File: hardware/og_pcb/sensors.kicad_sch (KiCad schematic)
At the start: 17 parts, among them U13 INA219AxD, U14 TMP1075DSG, U7 LSM303AGRTR

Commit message: updated pcb work in progress (incomplete)
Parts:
- removed C12, C14: 100nF, Capacitor_SMD:C_0402_1005Metric, symbol Device:C
- removed C13: 220nF, Capacitor_SMD:C_0402_1005Metric, symbol Device:C
- removed C41: 0.01uF, Capacitor_SMD:C_0402_1005Metric, symbol Device:C
- removed R10, R11, R18, R7: 10k, Resistor_SMD:R_0402_1005Metric, symbol Device:R
- removed R19, R20, R21: 5k, Resistor_SMD:R_0402_1005Metric, symbol Device:R
- removed U14: TMP1075DSG, Package_SON:WSON-8-1EP_2x2mm_P0.5mm_EP0.9x1.6mm_ThermalVias, symbol Sensor_Temperature:TMP1075DSG
- removed U7: LSM303AGRTR, 1my_footprints:SON_03AGRTR_STM-L, symbol 1my_symbol:LSM303AGR
- added C44: 0.01uF, Capacitor_SMD:C_0402_1005Metric, symbol Device:C
- added R24, R25, R26: 5k, Resistor_SMD:R_0402_1005Metric, symbol Device:R
- added U15: TMP1075DSG, Package_SON:WSON-8-1EP_2x2mm_P0.5mm_EP0.9x1.6mm_ThermalVias, symbol Sensor_Temperature:TMP1075DSG
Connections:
- net +3.3V: now also C44.1, R24.1, R25.1, R26.1, U15.8 (V+)
- net GND: now also C44.2, U15.4 (GND), U15.9 (EP)
- net Temp Alert: now also R26.2, U15.3 (ALERT)
- net at R22.1: now also U15.7 (A0)
- net Power Monitor SCL renamed SCL1
- net Power Monitor SDA renamed SDA1
- new net SCL0: R25.2, U15.2 (SCL), U15.5 (A2)
- new net SDA0: R24.2, U15.1 (SDA), U15.6 (A1)
- no-connect marks 3 -> 0
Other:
- note added: "add shunt resistor"
- note removed: "(pullup resistors)"
- note removed: "Inertial Measurement Unit"
- moved on the sheet: R22

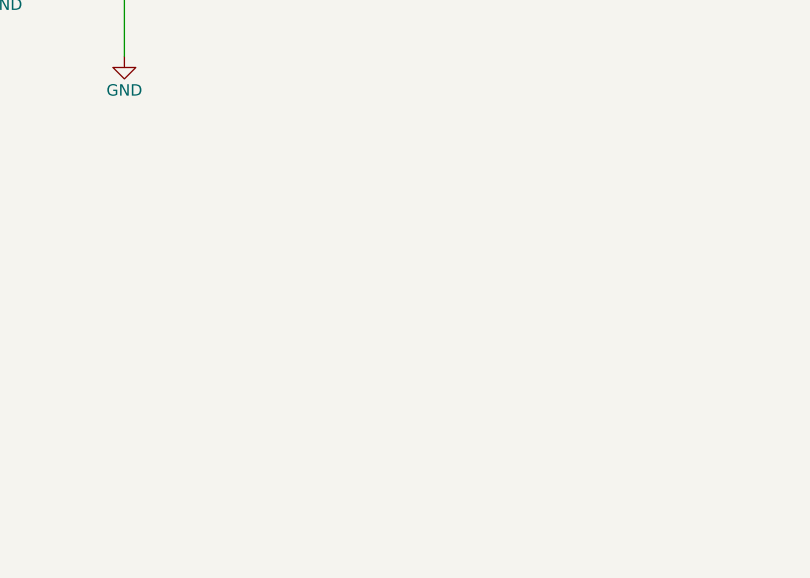
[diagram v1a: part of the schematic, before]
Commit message: updated pcb v2 progress
reimplemented spi microSD, changed power monitor to model with internal shunt resistor, changed power supply from usbc to barrel jack, reconnected vbus to microusb, modified spi and i2c connections (2 i2c connections, 2 spi connections), removed RF module & IMU.

to do:
- find/create footprints for new parts
- verify implementation by reviewing datasheets again
- implement coax connector for analog connection to cosmic watch
- implement gps receiver (must do more research; implement one well-known/documented/used b4)
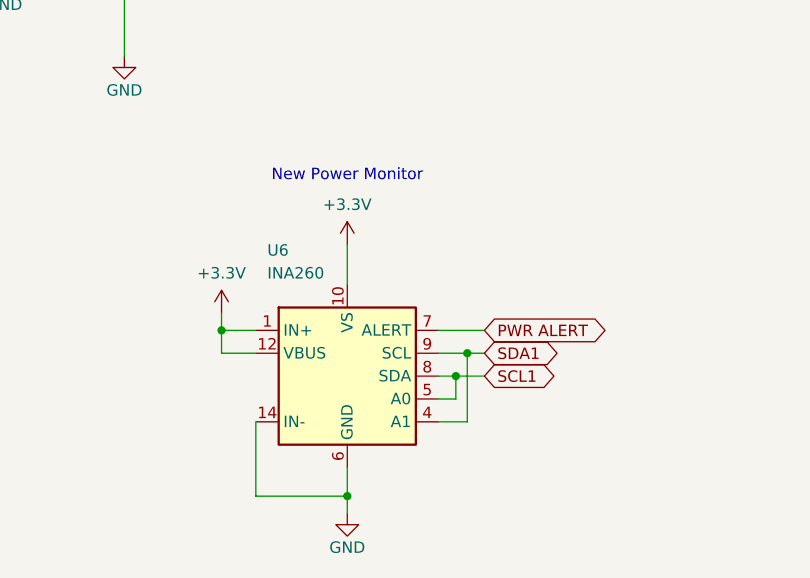
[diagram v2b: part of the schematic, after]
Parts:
- added U6: INA260, Package_SO:TSSOP-16_4.4x5mm_P0.65mm, symbol Sensor:INA260
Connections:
- net +3.3V: now also U6.1 (IN+), U6.10 (VS), U6.12 (VBUS), U6.2 (IN+), U6.3 (IN+)
- net GND: now also U6.11 (GND), U6.14 (IN-), U6.15 (IN-), U6.16 (IN-), U6.6 (GND)
- net SCL1: now also U6.5 (A0), U6.8 (SDA)
- net SDA1: now also U6.4 (A1), U6.9 (SCL)
- new net PWR ALERT: U6.7 (ALERT)
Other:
- note added: "New Power Monitor"

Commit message: new preliminary demo pcb
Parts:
- added C20: 10uF, Capacitor_SMD:C_0402_1005Metric, symbol Device:C
- added C21: 0.1uf, Capacitor_SMD:C_0402_1005Metric, symbol Device:C
- added FB1: FerriteBead, symbol Device:FerriteBead
- added J2: Conn_Coaxial, Connector_Coaxial:MMCX_Molex_73415-1471_Vertical, symbol Connector:Conn_Coaxial
- added R27: 0.002, Resistor_SMD:R_0402_1005Metric, symbol Device:R
- added U1: CD-PA1616D, 1my_footprints:CD-PA1616D, symbol CD-PA1616D:CD-PA1616D
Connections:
- net +3.3V: now also C20.1, C21.1, FB1.1, R27.1
- net GND: now also C20.2, C21.2, J2.2 (Ext), R27.2, U1.12 (GND), U1.19 (GND), U1.3 (GND), U1.8 (GND)
- net SCL1: now also U1.14 (RX1/I2C_SCL)
- net SDA1: now also U1.15 (TX1/I2C_SDA)
- new net: J2.1 (In), U1.11 (EX_ANT)
- new net: FB1.2, U1.1 (VCC)
- new net GPS Reset: U1.2 (~{RESET})
- no-connect marks 0 -> 5
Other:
- note added: "1pps pin provides one electrical pulse per second. Used to synchronize with other devices."
- note added: "3d-fix pin is led output"
- note added: "600 Ohms @ 100 MHz 1 Signal Line Ferrite Bead 0402 (1005 Metric) 200mA 650mOhm"
- note added: "Adafruit GPS/GNSS Receiver"
- note added: "Bypass capacitors for GPS receiver module VCC"
- note added: "GMLB-100505-0600A-N8"
- note added: "assign proper shunt resistor footprint"
- note added: "internal shunt resistor meaning no calibration needed"
- note added: "maybe connect vbackup to voltage supply 3.3v in case regular voltage supply pin is broken. add another capacitor nearby (1uf)"
- note added: "used to clean noise from power supply"
- note removed: "add shunt resistor"
- moved on the sheet: C17, C19, U6

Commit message: updated pcb
added footprints, led, testpoints
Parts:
- removed U6: INA260, Package_SO:TSSOP-16_4.4x5mm_P0.65mm, symbol Sensor:INA260
- added D2: LED, LED_SMD:LED_0603_1608Metric, symbol Device:LED
- added R28: 470, Resistor_SMD:R_0402_1005Metric, symbol Device:R
- added R29: 10k, Resistor_SMD:R_0402_1005Metric, symbol Device:R
- added TP1, TP3: TestPoint, 1my_footprints:TestPoint_Loop_D1.80mm_Drill1.0mm_Beaded, symbol Connector:TestPoint
- R27: footprint Resistor_SMD:R_0402_1005Metric -> Resistor_SMD:R_2512_6332Metric
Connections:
- net GND: now also D2.1 (K)
- net GPS Reset: now also R29.2
- net at J2.1 (In), U1.11 (EX_ANT): now also TP1.1
- net at FB1.2, U1.1 (VCC): now also R29.1, TP3.1
- net at U1.5 (3D-FIX): now also R28.1
- new net: D2.2 (A), R28.2
- no-connect marks 5 -> 4
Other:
- note added: "(add led)"
- note added: "(find or create a footprint for the ferrite bead)"
- note added: "Datasheet v0.5(one provided by adafruit):"
- note added: "Datasheet v0.6(provided by manufacturer):"
- note added: "https://cdn-shop.adafruit.com/product-files/1059/CD+PA1616D+Datasheet+v.05.pdf"
- note added: "https://drive.google.com/file/d/1kfhYX9w9B1p3TzluX87McfV2YKG-f-gQ/view"
- note added: "probably use the same shunt resistor used in the proves kit"
- note removed: "New Power Monitor"
- note removed: "internal shunt resistor meaning no calibration needed"
- moved on the sheet: FB1, J2

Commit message: pushed latest version
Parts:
- removed R26: 5k, Resistor_SMD:R_0402_1005Metric, symbol Device:R
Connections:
- net Temp Alert: no longer names the net of U15.3 (ALERT)
- no-connect marks 4 -> 5
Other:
- note added: "assign proper shunt resistor footprint (done)"
- note added: "removed temperature alert pin"
- note added: "tells if temp is too cold or too hot (outside of sensor's range in danger zone). This range will likely not be reached during demo except in the event we subject the pcb to extreme conditions."
- note added: "temp alert pin uses smbus protocol (dont know how to connect or implement, so will look into it more)"
- note removed: "assign proper shunt resistor footprint"
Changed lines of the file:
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@@
 	(generator_version "9.0")
 	(paper "A4")
+	(text "temp alert pin uses smbus protocol (dont know how to connect\nor implement, so will look into it more)"
+		(exclude_from_sim no)
+		(at 262.89 57.15 0)
+		(effects
+			(font
+				(size 1.27 1.27)
+			)
+		)
+	)
 	(text "maybe connect vbackup to voltage supply 3.3v in case\nregular voltage supply pin is broken. add another capacitor nearby (1uf)"
 		(exclude_from_sim no)
@@
 		)
 	)
+	(text "tells if temp is too cold or too hot (outside of sensor's range in danger zone).\nThis range will likely not be reached during demo except in the event we subject the pcb\nto extreme conditions."
+		(exclude_from_sim no)
+		(at 246.38 83.185 0)
+		(effects
+			(font
+				(size 1.27 1.27)
+			)
+		)
+	)
 	(text "Power Monitor"
 		(exclude_from_sim no)
@@
 		)
 	)
+	(text "removed temperature alert pin"
+		(exclude_from_sim no)
+		(at 230.505 71.12 0)
+		(effects
+			(font
+				(size 1.27 1.27)
+			)
+		)
+	)
 	(text "GMLB-100505-0600A-N8"
 		(exclude_from_sim no)
@@
 		)
 	)
-	(text "assign proper shunt resistor footprint"
+	(text "assign proper shunt resistor footprint\n(done)"
 		(exclude_from_sim no)
 		(at 42.545 62.865 0)
@@
 	)
 	(junction
-		(at 227.33 52.07)
-		(diameter 0)
-		(color 0 0 0 0)
-	)
-	(junction
 		(at 234.95 135.89)
 		(diameter 0)
@@
 	)
 	(junction
-		(at 234.315 69.215)
-		(diameter 0)
-		(color 0 0 0 0)
-	)
-	(junction
 		(at 200.025 77.47)
 		(diameter 0)
@@
 		(at 188.595 139.7)
 	)
-	(wire
-		(pts
-			(xy 234.315 69.215) (xy 212.725 69.215)
-		)
-		(stroke
-			(width 0)
-			(type default)
-		)
+	(no_connect
+		(at 212.725 69.215)
 	)
 	(wire
@@
 	(wire
 		(pts
-			(xy 234.315 52.07) (xy 234.315 61.595)
-		)
-		(stroke
-			(width 0)
-			(type default)
-		)
-	)
-	(wire
-		(pts
 			(xy 97.79 61.595) (xy 97.79 66.675)
 		)
@@
 	(wire
 		(pts
-			(xy 227.33 52.07) (xy 234.315 52.07)
-		)
-		(stroke
-			(width 0)
-			(type default)
-		)
-	)
-	(wire
-		(pts
 			(xy 83.82 49.53) (xy 83.82 53.975)
 		)
@@
 	(wire
 		(pts
-			(xy 240.03 69.215) (xy 234.315 69.215)
-		)
-		(stroke
-			(width 0)
-			(type default)
-		)
-	)
-	(wire
-		(pts
 			(xy 70.485 61.595) (xy 73.66 61.595)
 		)
@@
 		)
 	)
-	(global_label "Temp Alert"
-		(shape bidirectional)
-		(at 240.03 69.215 0)
-		(fields_autoplaced yes)
-		(effects
-			(font
-				(size 1.27 1.27)
-				(thickness 0.1588)
-			)
-			(justify left)
-		)
-		(property "Intersheetrefs" "${INTERSHEET_REFS}"
-			(at 254.3469 69.215 0)
-			(effects
-				(font
-					(size 1.27 1.27)
-				)
-				(justify left)
-				(hide yes)
-			)
-		)
-	)
 	(global_label "GPS Reset"
 		(shape input)
@@
 					(unit 1)
 				)
-			)
-		)
-	)
-	(symbol
-		(lib_id "Device:R")
-		(at 234.315 65.405 0)
-		(unit 1)
-		(exclude_from_sim no)
-		(in_bom yes)
-		(on_board yes)
-		(dnp no)
-		(property "Reference" "R26"
-			(at 236.22 64.135 0)
-			(effects
-				(font
-					(size 1.27 1.27)
-				)
-				(justify left)
-			)
-		)
-		(property "Value" "5k"
-			(at 236.22 66.675 0)
-			(effects
-				(font
-					(size 1.27 1.27)
-				)
-				(justify left)
-			)
-		)
-		(property "Footprint" "Resistor_SMD:R_0402_1005Metric"
-			(at 232.537 65.405 90)
-			(effects
-				(font
-					(size 1.27 1.27)
-				)
-				(hide yes)
-			)
-		)
-		(property "Datasheet" "~"
-			(at 234.315 65.405 0)
-			(effects
-				(font
-					(size 1.27 1.27)
-				)
-				(hide yes)
-			)
-		)
-		(property "Description" "Resistor"
-			(at 234.315 65.405 0)
-			(effects
-				(font
-					(size 1.27 1.27)
-				)
-				(hide yes)
-			)
-		)
-		(pin "1"
-		)
-		(pin "2"
-		)
-		(instances
-			(project "og_pcb"
-				(path "/e4ef350a-b140-44e0-8bc3-973fc24bf90a/3ccd8099-b4f2-4c2f-ac31-d7c505bfef59"
-					(reference "R26")
-					(unit 1)
-				)

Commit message: added comments from pragun's review
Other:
- note added: "(williams note)"
- note added: "connect the uart connections to RP2040"
- note added: "just put one decoupling capacitor (for the input positive shunt voltage)"
- note added: "remove the one for the power supply"
- note added: "see which speed is applicable for us and adjust resistor value"
- note added: "software support is mainly for UART, so change to UART implementation"
- note added: "temp alert pin uses smbus protocol"
- note added: "tie address pins to gnd and change resistors to 10k"
- note added: "tie the address pins to gnd or leave floating"
- note removed: "(add led)"
- note removed: "3d-fix pin is led output"
- note removed: "assign proper shunt resistor footprint (done)"
- note removed: "maybe connect vbackup to voltage supply 3.3v in case regular voltage supply pin is broken. add another capacitor nearby (1uf)"
- note removed: "probably use the same shunt resistor used in the proves kit"
- note removed: "temp alert pin uses smbus protocol (dont know how to connect or implement, so will look into it more)"
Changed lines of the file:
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@@
 	(generator_version "9.0")
 	(paper "A4")
-	(text "temp alert pin uses smbus protocol (dont know how to connect\nor implement, so will look into it more)"
+	(text "temp alert pin uses smbus protocol\n"
 		(exclude_from_sim no)
 		(at 262.89 57.15 0)
@@
 		)
 	)
-	(text "maybe connect vbackup to voltage supply 3.3v in case\nregular voltage supply pin is broken. add another capacitor nearby (1uf)"
-		(exclude_from_sim no)
-		(at 198.12 149.225 0)
-		(effects
-			(font
-				(size 1.27 1.27)
-			)
-		)
-	)
 	(text "tells if temp is too cold or too hot (outside of sensor's range in danger zone).\nThis range will likely not be reached during demo except in the event we subject the pcb\nto extreme conditions."
 		(exclude_from_sim no)
@@
 		)
 	)
-	(text "3d-fix pin is led output"
-		(exclude_from_sim no)
-		(at 157.48 142.24 0)
+	(text "see which speed is applicable for us and adjust resistor value"
+		(exclude_from_sim no)
+		(at 155.575 62.23 0)
 		(effects
 			(font
@@
 		)
 	)
+	(text "(williams note)"
+		(exclude_from_sim no)
+		(at 243.205 78.105 0)
+		(effects
+			(font
+				(size 1.27 1.27)
+			)
+		)
+	)
 	(text "Temperature Sensor"
 		(exclude_from_sim no)
@@
 		)
 	)
-	(text "assign proper shunt resistor footprint\n(done)"
-		(exclude_from_sim no)
-		(at 42.545 62.865 0)
-		(effects
-			(font
-				(size 1.27 1.27)
-			)
-		)
-	)
 	(text "1pps pin provides one electrical pulse per second.\nUsed to synchronize with other devices."
 		(exclude_from_sim no)
@@
 		)
 	)
+	(text "just put one decoupling capacitor (for the input positive shunt voltage)"
+		(exclude_from_sim no)
+		(at 114.3 24.765 0)
+		(effects
+			(font
+				(size 1.27 1.27)
+			)
+		)
+	)
 	(text "(find or create a footprint for the ferrite bead)"
 		(exclude_from_sim no)
@@
 		)
 	)
+	(text "software support is mainly for UART, so change to UART\nimplementation\n"
+		(exclude_from_sim no)
+		(at 259.08 139.065 0)
+		(effects
+			(font
+				(size 1.27 1.27)
+			)
+		)
+	)
 	(text "Bypass capacitors for GPS receiver module\nVCC\n"
 		(exclude_from_sim no)
@@
 		)
 	)
-	(text "(add led)"
-		(exclude_from_sim no)
-		(at 157.48 145.415 0)
-		(effects
-			(font
-				(size 1.27 1.27)
-			)
-		)
-	)
-	(text "probably use the same shunt resistor used in the proves kit"
-		(exclude_from_sim no)
-		(at 40.005 69.215 0)
+	(text "connect the uart connections to RP2040"
+		(exclude_from_sim no)
+		(at 258.445 132.715 0)
+		(effects
+			(font
+				(size 1.27 1.27)
+			)
+		)
+	)
+	(text "remove the one for the power supply"
+		(exclude_from_sim no)
+		(at 103.505 29.21 0)
+		(effects
+			(font
+				(size 1.27 1.27)
+			)
+		)
+	)
+	(text "tie the address pins to gnd or leave floating"
+		(exclude_from_sim no)
+		(at 95.885 76.2 0)
 		(effects
 			(font
@@
 		(effects
 			(font
+				(size 1.27 1.27)
+			)
+		)
+	)
+	(text "tie address pins to gnd and change resistors to 10k"
+		(exclude_from_sim no)
+		(at 161.29 59.055 0)
+		(effects
+			(font
